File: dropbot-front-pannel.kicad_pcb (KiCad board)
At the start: 4 copper layers, 108.3 x 68.8 mm, 28 parts, among them P1 SFM-105-02-L-D-A, P10 CONN_01X02, P11 USB_A, P12 USB_B, P13 CONN_01X01, P14 CONN_01X01, P15 CONN_01X01, P2 SFM-125-02-L-D-A, P3 TFM-125-02-L-DH, P4 SFM-125-02-L-D-A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

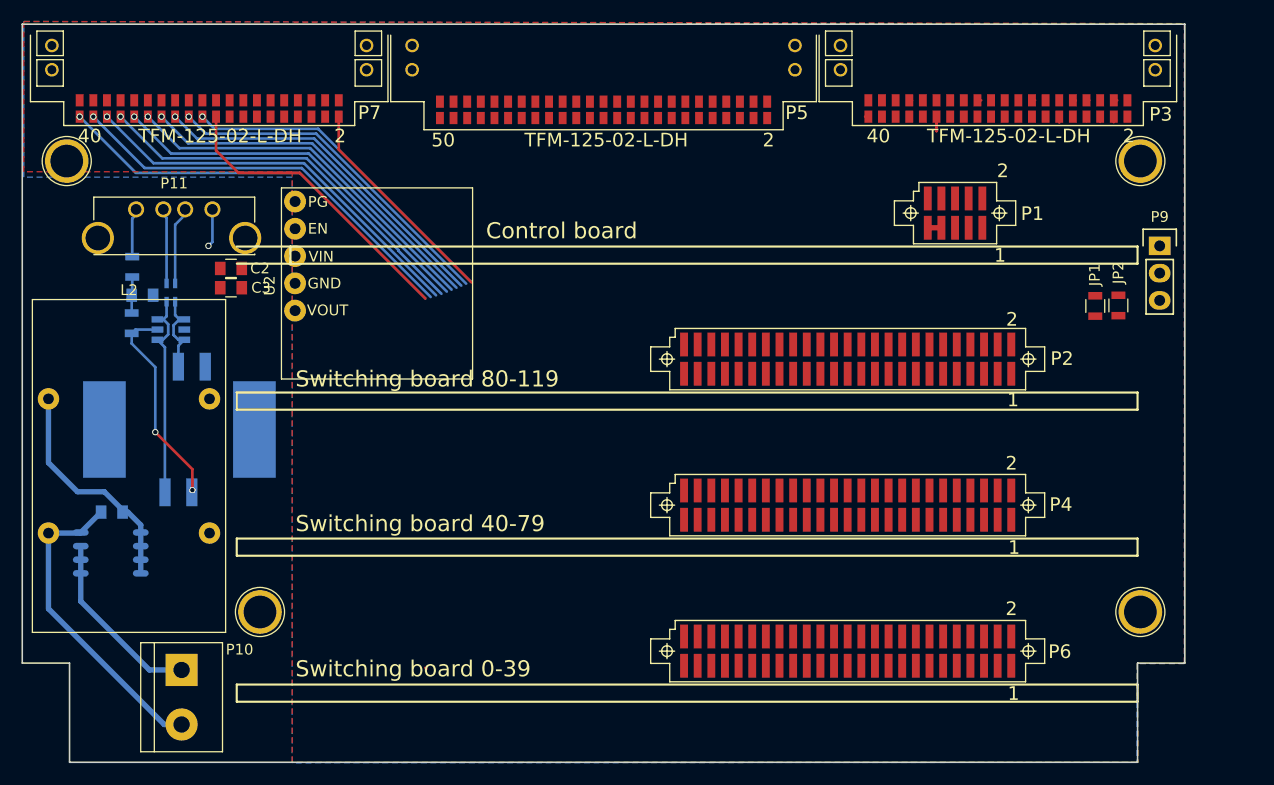
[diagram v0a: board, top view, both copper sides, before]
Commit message: [WIP] route HV outputs
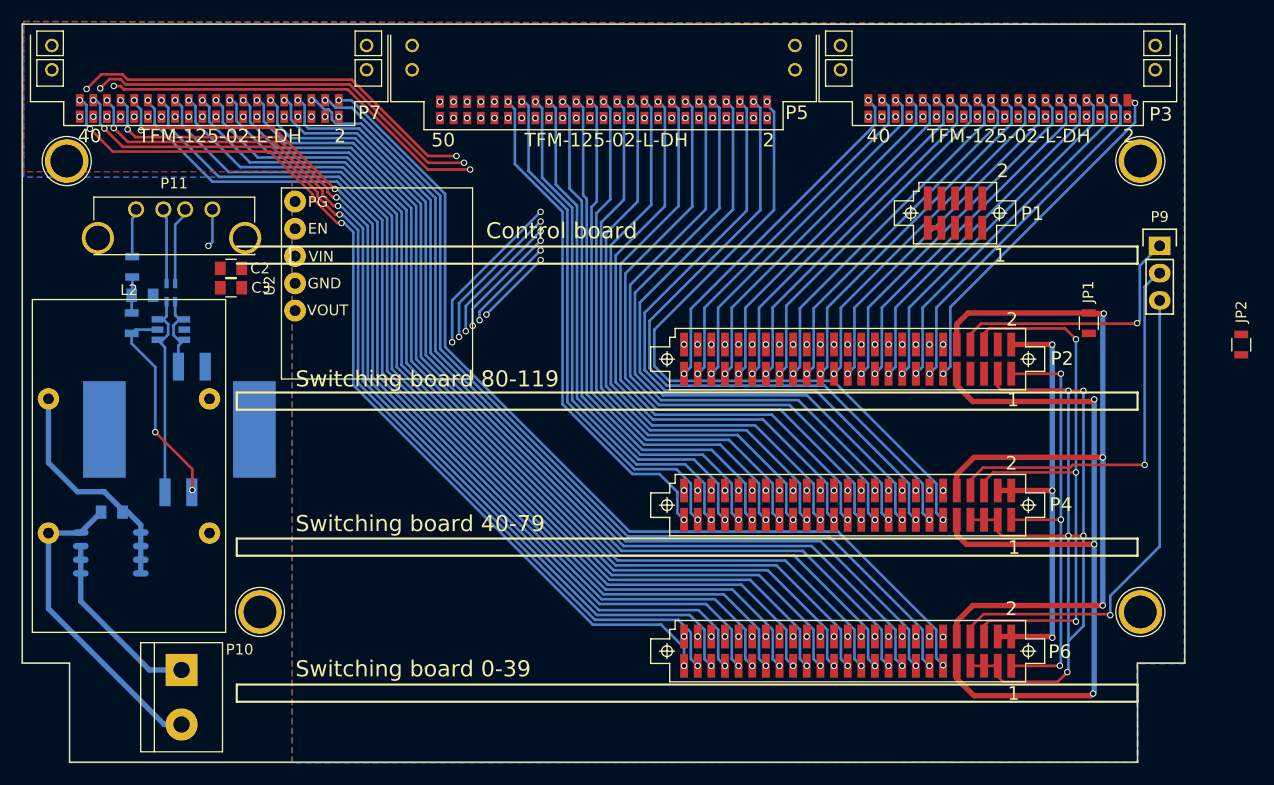
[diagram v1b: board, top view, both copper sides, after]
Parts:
- moved JP2 12.0 mm to (159.4, 61.1)
- moved JP1 1.71 mm to (145.2, 59.1)
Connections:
- P3 pad 1: HVOUT0 -> HVOUT39
- P3 pad 10: HVOUT9 -> HVOUT30
- P3 pad 11: HVOUT10 -> HVOUT29
- P3 pad 12: HVOUT11 -> HVOUT28
- P3 pad 13: HVOUT12 -> HVOUT27
- P3 pad 14: HVOUT13 -> HVOUT26
- P3 pad 15: HVOUT14 -> HVOUT25
- P3 pad 16: HVOUT15 -> HVOUT24
- P3 pad 17: HVOUT16 -> HVOUT23
- P3 pad 18: HVOUT17 -> HVOUT22
- P3 pad 19: HVOUT18 -> HVOUT21
- P3 pad 2: HVOUT1 -> HVOUT38
- P3 pad 20: HVOUT19 -> HVOUT20
- P3 pad 21: HVOUT20 -> HVOUT19
- P3 pad 22: HVOUT21 -> HVOUT18
- P3 pad 23: HVOUT22 -> HVOUT17
- P3 pad 24: HVOUT23 -> HVOUT16
- P3 pad 25: HVOUT24 -> HVOUT15
- P3 pad 26: HVOUT25 -> HVOUT14
- P3 pad 27: HVOUT26 -> HVOUT13
- P3 pad 28: HVOUT27 -> HVOUT12
- P3 pad 29: HVOUT28 -> HVOUT11
- P3 pad 3: HVOUT2 -> HVOUT37
- P3 pad 30: HVOUT29 -> HVOUT10
- P3 pad 31: HVOUT30 -> HVOUT9
- P3 pad 32: HVOUT31 -> HVOUT8
- P3 pad 33: HVOUT32 -> HVOUT7
- P3 pad 34: HVOUT33 -> HVOUT6
- P3 pad 35: HVOUT34 -> HVOUT5
- P3 pad 36: HVOUT35 -> HVOUT4
- P3 pad 37: HVOUT36 -> HVOUT3
- P3 pad 38: HVOUT37 -> HVOUT2
- P3 pad 39: HVOUT38 -> HVOUT1
- P3 pad 4: HVOUT3 -> HVOUT36
- P3 pad 40: HVOUT39 -> HVOUT0
- P3 pad 5: HVOUT4 -> HVOUT35
- P3 pad 6: HVOUT5 -> HVOUT34
- P3 pad 7: HVOUT6 -> HVOUT33
- P3 pad 8: HVOUT7 -> HVOUT32
- P3 pad 9: HVOUT8 -> HVOUT31
- P5 pad 1: HVOUT40 -> HVOUT79
- P5 pad 10: HVOUT49 -> HVOUT70
- P5 pad 11: HVOUT50 -> HVOUT69
- P5 pad 12: HVOUT51 -> HVOUT68
- P5 pad 13: HVOUT52 -> HVOUT67
- P5 pad 14: HVOUT53 -> HVOUT66
- P5 pad 15: HVOUT54 -> HVOUT65
- P5 pad 16: HVOUT55 -> HVOUT64
- P5 pad 17: HVOUT56 -> HVOUT63
- P5 pad 18: HVOUT57 -> HVOUT62
- P5 pad 19: HVOUT58 -> HVOUT61
- P5 pad 2: HVOUT41 -> HVOUT78
- P5 pad 20: HVOUT59 -> HVOUT60
- P5 pad 21: HVOUT60 -> HVOUT59
- P5 pad 22: HVOUT61 -> HVOUT58
- P5 pad 23: HVOUT62 -> HVOUT57
- P5 pad 24: HVOUT63 -> HVOUT56
- P5 pad 25: HVOUT64 -> HVOUT55
- P5 pad 26: HVOUT65 -> HVOUT54
- P5 pad 27: HVOUT66 -> HVOUT53
- P5 pad 28: HVOUT67 -> HVOUT52
- P5 pad 29: HVOUT68 -> HVOUT51
- P5 pad 3: HVOUT42 -> HVOUT77
- P5 pad 30: HVOUT69 -> HVOUT50
- P5 pad 31: HVOUT70 -> HVOUT49
- P5 pad 32: HVOUT71 -> HVOUT48
- P5 pad 33: HVOUT72 -> HVOUT47
- P5 pad 34: HVOUT73 -> HVOUT46
- P5 pad 35: HVOUT74 -> HVOUT45
- P5 pad 36: HVOUT75 -> HVOUT44
- P5 pad 37: HVOUT76 -> HVOUT43
- P5 pad 38: HVOUT77 -> HVOUT42
- P5 pad 39: HVOUT78 -> HVOUT41
- P5 pad 4: HVOUT43 -> HVOUT76
- P5 pad 40: HVOUT79 -> HVOUT40
- P5 pad 5: HVOUT44 -> HVOUT75
- P5 pad 6: HVOUT45 -> HVOUT74
- P5 pad 7: HVOUT46 -> HVOUT73
- P5 pad 8: HVOUT47 -> HVOUT72
- P5 pad 9: HVOUT48 -> HVOUT71
- P7 pad 1: HVOUT80 -> HVOUT119
- P7 pad 10: HVOUT89 -> HVOUT110
- P7 pad 11: HVOUT90 -> HVOUT109
- P7 pad 12: HVOUT91 -> HVOUT108
- P7 pad 13: HVOUT92 -> HVOUT107
- P7 pad 14: HVOUT93 -> HVOUT106
- P7 pad 15: HVOUT94 -> HVOUT105
- P7 pad 16: HVOUT95 -> HVOUT104
- P7 pad 17: HVOUT96 -> HVOUT103
- P7 pad 18: HVOUT97 -> HVOUT102
- P7 pad 19: HVOUT98 -> HVOUT101
- P7 pad 2: HVOUT81 -> HVOUT118
- P7 pad 20: HVOUT99 -> HVOUT100
- P7 pad 21: HVOUT100 -> HVOUT99
- P7 pad 22: HVOUT101 -> HVOUT98
- P7 pad 23: HVOUT102 -> HVOUT97
- P7 pad 24: HVOUT103 -> HVOUT96
- P7 pad 25: HVOUT104 -> HVOUT95
- P7 pad 26: HVOUT105 -> HVOUT94
- P7 pad 27: HVOUT106 -> HVOUT93
- P7 pad 28: HVOUT107 -> HVOUT92
- P7 pad 29: HVOUT108 -> HVOUT91
- P7 pad 3: HVOUT82 -> HVOUT117
- P7 pad 30: HVOUT109 -> HVOUT90
- P7 pad 31: HVOUT110 -> HVOUT89
- P7 pad 32: HVOUT111 -> HVOUT88
- P7 pad 33: HVOUT112 -> HVOUT87
- P7 pad 34: HVOUT113 -> HVOUT86
- P7 pad 35: HVOUT114 -> HVOUT85
- P7 pad 36: HVOUT115 -> HVOUT84
- P7 pad 37: HVOUT116 -> HVOUT83
- P7 pad 38: HVOUT117 -> HVOUT82
- P7 pad 39: HVOUT118 -> HVOUT81
- P7 pad 4: HVOUT83 -> HVOUT116
- P7 pad 40: HVOUT119 -> HVOUT80
- P7 pad 5: HVOUT84 -> HVOUT115
- P7 pad 6: HVOUT85 -> HVOUT114
- P7 pad 7: HVOUT86 -> HVOUT113
- P7 pad 8: HVOUT87 -> HVOUT112
- P7 pad 9: HVOUT88 -> HVOUT111
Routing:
- net HVOUT80: track 0.00 -> 106.0 mm, vias 0 -> 6
- net HVOUT82: track 0.00 -> 104.2 mm, vias 0 -> 6
- net HVOUT84: track 0.00 -> 102.3 mm, vias 0 -> 6
- net HVOUT86: track 0.00 -> 100.9 mm, vias 0 -> 4
- net HVOUT88: track 0.00 -> 98.8 mm, vias 0 -> 4
- net HVOUT90: track 0.00 -> 97.0 mm, vias 0 -> 4
- net HVOUT89: track 0.00 -> 89.7 mm, vias 0 -> 4
- net HVOUT87: track 0.00 -> 89.5 mm, vias 0 -> 4
- net HVOUT85: track 0.00 -> 89.4 mm, vias 0 -> 4
- net HVOUT83: track 0.00 -> 89.2 mm, vias 0 -> 4
- net HVOUT93: track 0.00 -> 89.1 mm, vias 0 -> 2
- net HVOUT95: track 0.00 -> 89.1 mm, vias 0 -> 2
- net HVOUT91: track 0.00 -> 89.0 mm, vias 0 -> 2
- net HVOUT97: track 0.00 -> 89.0 mm, vias 0 -> 2
- net HVOUT92: track 0.00 -> 84.6 mm, vias 0 -> 2
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- added copper zone on PWR, net GND

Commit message: [WIP] swap order of switching boards
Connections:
- P2 pad 11: HVOUT39 -> HVOUT119
- P2 pad 12: HVOUT38 -> HVOUT118
- P2 pad 13: HVOUT37 -> HVOUT117
- P2 pad 14: HVOUT36 -> HVOUT116
- P2 pad 15: HVOUT35 -> HVOUT115
- P2 pad 16: HVOUT34 -> HVOUT114
- P2 pad 17: HVOUT33 -> HVOUT113
- P2 pad 18: HVOUT32 -> HVOUT112
- P2 pad 19: HVOUT31 -> HVOUT111
- P2 pad 20: HVOUT30 -> HVOUT110
- P2 pad 21: HVOUT29 -> HVOUT109
- P2 pad 22: HVOUT28 -> HVOUT108
- P2 pad 23: HVOUT27 -> HVOUT107
- P2 pad 24: HVOUT26 -> HVOUT106
- P2 pad 25: HVOUT25 -> HVOUT105
- P2 pad 26: HVOUT24 -> HVOUT104
- P2 pad 27: HVOUT23 -> HVOUT103
- P2 pad 28: HVOUT22 -> HVOUT102
- P2 pad 29: HVOUT21 -> HVOUT101
- P2 pad 30: HVOUT20 -> HVOUT100
- P2 pad 31: HVOUT19 -> HVOUT99
- P2 pad 32: HVOUT18 -> HVOUT98
- P2 pad 33: HVOUT17 -> HVOUT97
- P2 pad 34: HVOUT16 -> HVOUT96
- P2 pad 35: HVOUT15 -> HVOUT95
- P2 pad 36: HVOUT14 -> HVOUT94
- P2 pad 37: HVOUT13 -> HVOUT93
- P2 pad 38: HVOUT12 -> HVOUT92
- P2 pad 39: HVOUT11 -> HVOUT91
- P2 pad 40: HVOUT10 -> HVOUT90
- P2 pad 41: HVOUT9 -> HVOUT89
- P2 pad 42: HVOUT8 -> HVOUT88
- P2 pad 43: HVOUT7 -> HVOUT87
- P2 pad 44: HVOUT6 -> HVOUT86
- P2 pad 45: HVOUT5 -> HVOUT85
- P2 pad 46: HVOUT4 -> HVOUT84
- P2 pad 47: HVOUT3 -> HVOUT83
- P2 pad 48: HVOUT2 -> HVOUT82
- P2 pad 49: HVOUT1 -> HVOUT81
- P2 pad 50: HVOUT0 -> HVOUT80
- P2 pad 8: RST1 -> RST3
- P3 pad 1: HVOUT39 -> HVOUT119
- P3 pad 10: HVOUT30 -> HVOUT110
- P3 pad 11: HVOUT29 -> HVOUT109
- P3 pad 12: HVOUT28 -> HVOUT108
- P3 pad 13: HVOUT27 -> HVOUT107
- P3 pad 14: HVOUT26 -> HVOUT106
- P3 pad 15: HVOUT25 -> HVOUT105
- P3 pad 16: HVOUT24 -> HVOUT104
- P3 pad 17: HVOUT23 -> HVOUT103
- P3 pad 18: HVOUT22 -> HVOUT102
- P3 pad 19: HVOUT21 -> HVOUT101
- P3 pad 2: HVOUT38 -> HVOUT118
- P3 pad 20: HVOUT20 -> HVOUT100
- P3 pad 21: HVOUT19 -> HVOUT99
- P3 pad 22: HVOUT18 -> HVOUT98
- P3 pad 23: HVOUT17 -> HVOUT97
- P3 pad 24: HVOUT16 -> HVOUT96
- P3 pad 25: HVOUT15 -> HVOUT95
- P3 pad 26: HVOUT14 -> HVOUT94
- P3 pad 27: HVOUT13 -> HVOUT93
- P3 pad 28: HVOUT12 -> HVOUT92
- P3 pad 29: HVOUT11 -> HVOUT91
- P3 pad 3: HVOUT37 -> HVOUT117
- P3 pad 30: HVOUT10 -> HVOUT90
- P3 pad 31: HVOUT9 -> HVOUT89
- P3 pad 32: HVOUT8 -> HVOUT88
- P3 pad 33: HVOUT7 -> HVOUT87
- P3 pad 34: HVOUT6 -> HVOUT86
- P3 pad 35: HVOUT5 -> HVOUT85
- P3 pad 36: HVOUT4 -> HVOUT84
- P3 pad 37: HVOUT3 -> HVOUT83
- P3 pad 38: HVOUT2 -> HVOUT82
- P3 pad 39: HVOUT1 -> HVOUT81
- P3 pad 4: HVOUT36 -> HVOUT116
- P3 pad 40: HVOUT0 -> HVOUT80
- P3 pad 5: HVOUT35 -> HVOUT115
- P3 pad 6: HVOUT34 -> HVOUT114
- P3 pad 7: HVOUT33 -> HVOUT113
- P3 pad 8: HVOUT32 -> HVOUT112
- P3 pad 9: HVOUT31 -> HVOUT111
- P6 pad 11: HVOUT119 -> HVOUT39
- P6 pad 12: HVOUT118 -> HVOUT38
- P6 pad 13: HVOUT117 -> HVOUT37
- P6 pad 14: HVOUT116 -> HVOUT36
- P6 pad 15: HVOUT115 -> HVOUT35
- P6 pad 16: HVOUT114 -> HVOUT34
- P6 pad 17: HVOUT113 -> HVOUT33
- P6 pad 18: HVOUT112 -> HVOUT32
- P6 pad 19: HVOUT111 -> HVOUT31
- P6 pad 20: HVOUT110 -> HVOUT30
- P6 pad 21: HVOUT109 -> HVOUT29
- P6 pad 22: HVOUT108 -> HVOUT28
- P6 pad 23: HVOUT107 -> HVOUT27
- P6 pad 24: HVOUT106 -> HVOUT26
- P6 pad 25: HVOUT105 -> HVOUT25
- P6 pad 26: HVOUT104 -> HVOUT24
- P6 pad 27: HVOUT103 -> HVOUT23
- P6 pad 28: HVOUT102 -> HVOUT22
- P6 pad 29: HVOUT101 -> HVOUT21
- P6 pad 30: HVOUT100 -> HVOUT20
- P6 pad 31: HVOUT99 -> HVOUT19
- P6 pad 32: HVOUT98 -> HVOUT18
- P6 pad 33: HVOUT97 -> HVOUT17
- P6 pad 34: HVOUT96 -> HVOUT16
- P6 pad 35: HVOUT95 -> HVOUT15
- P6 pad 36: HVOUT94 -> HVOUT14
- P6 pad 37: HVOUT93 -> HVOUT13
- P6 pad 38: HVOUT92 -> HVOUT12
- P6 pad 39: HVOUT91 -> HVOUT11
- P6 pad 40: HVOUT90 -> HVOUT10
- P6 pad 41: HVOUT89 -> HVOUT9
- P6 pad 42: HVOUT88 -> HVOUT8
- P6 pad 43: HVOUT87 -> HVOUT7
- P6 pad 44: HVOUT86 -> HVOUT6
- P6 pad 45: HVOUT85 -> HVOUT5
- P6 pad 46: HVOUT84 -> HVOUT4
- P6 pad 47: HVOUT83 -> HVOUT3
- P6 pad 48: HVOUT82 -> HVOUT2
- P6 pad 49: HVOUT81 -> HVOUT1
- P6 pad 50: HVOUT80 -> HVOUT0
- P6 pad 8: RST3 -> RST1
- P7 pad 1: HVOUT119 -> HVOUT39
- P7 pad 10: HVOUT110 -> HVOUT30
- P7 pad 11: HVOUT109 -> HVOUT29
- P7 pad 12: HVOUT108 -> HVOUT28
- P7 pad 13: HVOUT107 -> HVOUT27
- P7 pad 14: HVOUT106 -> HVOUT26
- P7 pad 15: HVOUT105 -> HVOUT25
- P7 pad 16: HVOUT104 -> HVOUT24
- P7 pad 17: HVOUT103 -> HVOUT23
- P7 pad 18: HVOUT102 -> HVOUT22
- P7 pad 19: HVOUT101 -> HVOUT21
- P7 pad 2: HVOUT118 -> HVOUT38
- P7 pad 20: HVOUT100 -> HVOUT20
- P7 pad 21: HVOUT99 -> HVOUT19
- P7 pad 22: HVOUT98 -> HVOUT18
- P7 pad 23: HVOUT97 -> HVOUT17
- P7 pad 24: HVOUT96 -> HVOUT16
- P7 pad 25: HVOUT95 -> HVOUT15
- P7 pad 26: HVOUT94 -> HVOUT14
- P7 pad 27: HVOUT93 -> HVOUT13
- P7 pad 28: HVOUT92 -> HVOUT12
- P7 pad 29: HVOUT91 -> HVOUT11
- P7 pad 3: HVOUT117 -> HVOUT37
- P7 pad 30: HVOUT90 -> HVOUT10
- P7 pad 31: HVOUT89 -> HVOUT9
- P7 pad 32: HVOUT88 -> HVOUT8
- P7 pad 33: HVOUT87 -> HVOUT7
- P7 pad 34: HVOUT86 -> HVOUT6
- P7 pad 35: HVOUT85 -> HVOUT5
- P7 pad 36: HVOUT84 -> HVOUT4
- P7 pad 37: HVOUT83 -> HVOUT3
- P7 pad 38: HVOUT82 -> HVOUT2
- P7 pad 39: HVOUT81 -> HVOUT1
- P7 pad 4: HVOUT116 -> HVOUT36
- P7 pad 40: HVOUT80 -> HVOUT0
- P7 pad 5: HVOUT115 -> HVOUT35
- P7 pad 6: HVOUT114 -> HVOUT34
- P7 pad 7: HVOUT113 -> HVOUT33
- P7 pad 8: HVOUT112 -> HVOUT32
- P7 pad 9: HVOUT111 -> HVOUT31
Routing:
- net HVOUT80: track 106.0 -> 28.4 mm, vias 6 -> 2
- net HVOUT0: track 28.4 -> 106.0 mm, vias 2 -> 6
- net HVOUT82: track 104.2 -> 28.4 mm, vias 6 -> 2
- net HVOUT2: track 28.4 -> 104.2 mm, vias 2 -> 6
- net HVOUT84: track 102.3 -> 28.4 mm, vias 6 -> 2
- net HVOUT4: track 28.4 -> 102.3 mm, vias 2 -> 6
- net HVOUT86: track 100.9 -> 28.4 mm, vias 4 -> 2
- net HVOUT6: track 28.4 -> 100.9 mm, vias 2 -> 4
- net HVOUT88: track 98.8 -> 28.4 mm, vias 4 -> 2
- net HVOUT8: track 28.4 -> 98.8 mm, vias 2 -> 4
- net HVOUT90: track 97.0 -> 28.6 mm, vias 4 -> 2
- net HVOUT10: track 28.6 -> 97.0 mm, vias 2 -> 4
- net HVOUT9: track 33.2 -> 89.7 mm, vias 2 -> 4
- net HVOUT89: track 89.7 -> 33.2 mm, vias 4 -> 2
- net HVOUT87: track 89.5 -> 33.2 mm, vias 4 -> 2
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
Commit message: [WIP] route power, ground planes
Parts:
- moved JP2 31.6 mm to (132.2, 45.1), turned to 180 degrees
- moved P9 5.10 mm to (151.8, 57.0), turned to 180 degrees
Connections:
- P3 pad G1: Net-(P3-PadG1) -> GND
- P3 pad G2: Net-(P3-PadG1) -> GND
- P3 pad G3: Net-(P3-PadG1) -> GND
- P3 pad G4: Net-(P3-PadG1) -> GND
- P5 pad 1: HVOUT79 -> Net-(P5-Pad1)
- P5 pad 10: HVOUT70 -> Net-(P5-Pad10)
- P5 pad 11: HVOUT69 -> HVOUT79
- P5 pad 12: HVOUT68 -> HVOUT78
- P5 pad 13: HVOUT67 -> HVOUT77
- P5 pad 14: HVOUT66 -> HVOUT76
- P5 pad 15: HVOUT65 -> HVOUT75
- P5 pad 16: HVOUT64 -> HVOUT74
- P5 pad 17: HVOUT63 -> HVOUT73
- P5 pad 18: HVOUT62 -> HVOUT72
- P5 pad 19: HVOUT61 -> HVOUT71
- P5 pad 2: HVOUT78 -> Net-(P5-Pad2)
- P5 pad 20: HVOUT60 -> HVOUT70
- P5 pad 21: HVOUT59 -> HVOUT69
- P5 pad 22: HVOUT58 -> HVOUT68
- P5 pad 23: HVOUT57 -> HVOUT67
- P5 pad 24: HVOUT56 -> HVOUT66
- P5 pad 25: HVOUT55 -> HVOUT65
- P5 pad 26: HVOUT54 -> HVOUT64
- P5 pad 27: HVOUT53 -> HVOUT63
- P5 pad 28: HVOUT52 -> HVOUT62
- P5 pad 29: HVOUT51 -> HVOUT61
- P5 pad 3: HVOUT77 -> Net-(P5-Pad3)
- P5 pad 30: HVOUT50 -> HVOUT60
- P5 pad 31: HVOUT49 -> HVOUT59
- P5 pad 32: HVOUT48 -> HVOUT58
- P5 pad 33: HVOUT47 -> HVOUT57
- P5 pad 34: HVOUT46 -> HVOUT56
- P5 pad 35: HVOUT45 -> HVOUT55
- P5 pad 36: HVOUT44 -> HVOUT54
- P5 pad 37: HVOUT43 -> HVOUT53
- P5 pad 38: HVOUT42 -> HVOUT52
- P5 pad 39: HVOUT41 -> HVOUT51
- P5 pad 4: HVOUT76 -> Net-(P5-Pad4)
- P5 pad 40: HVOUT40 -> HVOUT50
- P5 pad 41: Net-(P5-Pad41) -> HVOUT49
- P5 pad 42: Net-(P5-Pad42) -> HVOUT48
- P5 pad 43: Net-(P5-Pad43) -> HVOUT47
- P5 pad 44: Net-(P5-Pad44) -> HVOUT46
- P5 pad 45: Net-(P5-Pad45) -> HVOUT45
- P5 pad 46: Net-(P5-Pad46) -> HVOUT44
- P5 pad 47: Net-(P5-Pad47) -> HVOUT43
- P5 pad 48: Net-(P5-Pad48) -> HVOUT42
- P5 pad 49: Net-(P5-Pad49) -> HVOUT41
- P5 pad 5: HVOUT75 -> Net-(P5-Pad5)
- P5 pad 50: Net-(P5-Pad50) -> HVOUT40
- P5 pad 6: HVOUT74 -> Net-(P5-Pad6)
- P5 pad 7: HVOUT73 -> Net-(P5-Pad7)
- P5 pad 8: HVOUT72 -> Net-(P5-Pad8)
- P5 pad 9: HVOUT71 -> Net-(P5-Pad9)
- P5 pad G1: Net-(P5-PadG1) -> GND
- P5 pad G2: Net-(P5-PadG1) -> GND
- P5 pad G3: Net-(P5-PadG1) -> GND
- P5 pad G4: Net-(P5-PadG1) -> GND
- P7 pad G1: Net-(P7-PadG1) -> GND
- P7 pad G2: Net-(P7-PadG1) -> GND
- P7 pad G3: Net-(P7-PadG1) -> GND
- P7 pad G4: Net-(P7-PadG1) -> GND
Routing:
- net GND: track 85.4 -> 177.0 mm, vias 6 -> 12
- net HVAC: track 71.2 -> 111.5 mm, vias 3 -> 4
- net +12V: track 1.42 -> 37.7 mm, vias 0 -> 3
- net SCL: track 58.8 -> 83.8 mm, vias 3 -> 4
- net SDA: track 41.0 -> 61.9 mm, vias 3 -> 4
- net +3.3V: track 41.4 -> 21.6 mm, vias 3 -> 7
- net RST3: track 40.2 -> 25.0 mm
- net RST1: track 31.4 -> 46.2 mm
- net CHASIS_GND: track 29.6 -> 43.9 mm, vias 0 -> 9
- net HVOUT40: track 43.5 -> 47.8 mm
- net HVOUT42: track 43.9 -> 47.9 mm
- net HVOUT41: track 47.2 -> 50.7 mm
- net HVOUT44: track 44.2 -> 47.5 mm
- net HVOUT45: track 48.4 -> 51.7 mm
- net HVOUT43: track 48.2 -> 51.4 mm
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- added copper zone on F.Cu, net +12V
- added copper zone on PWR, net +12V
- added copper zone on PWR, net +3.3V
